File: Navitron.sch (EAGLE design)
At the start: 78 parts, among them J2 DX07S016JA1R1500, Q1 ROHM_RUM002N02T2LROHM_RUM002N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, Q2 2.5A/30V, Q3 ROHM_RUM002N02T2LROHM_RUM002N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, Q4 ROHM_RUM002N02T2LROHM_RUM002N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, Q5 ROHM_RUM002N02T2LROHM_RUM002N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, T1 BC847, T2 BC847, U1 ESP32-WROOM-32, U2 9DoF IMU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

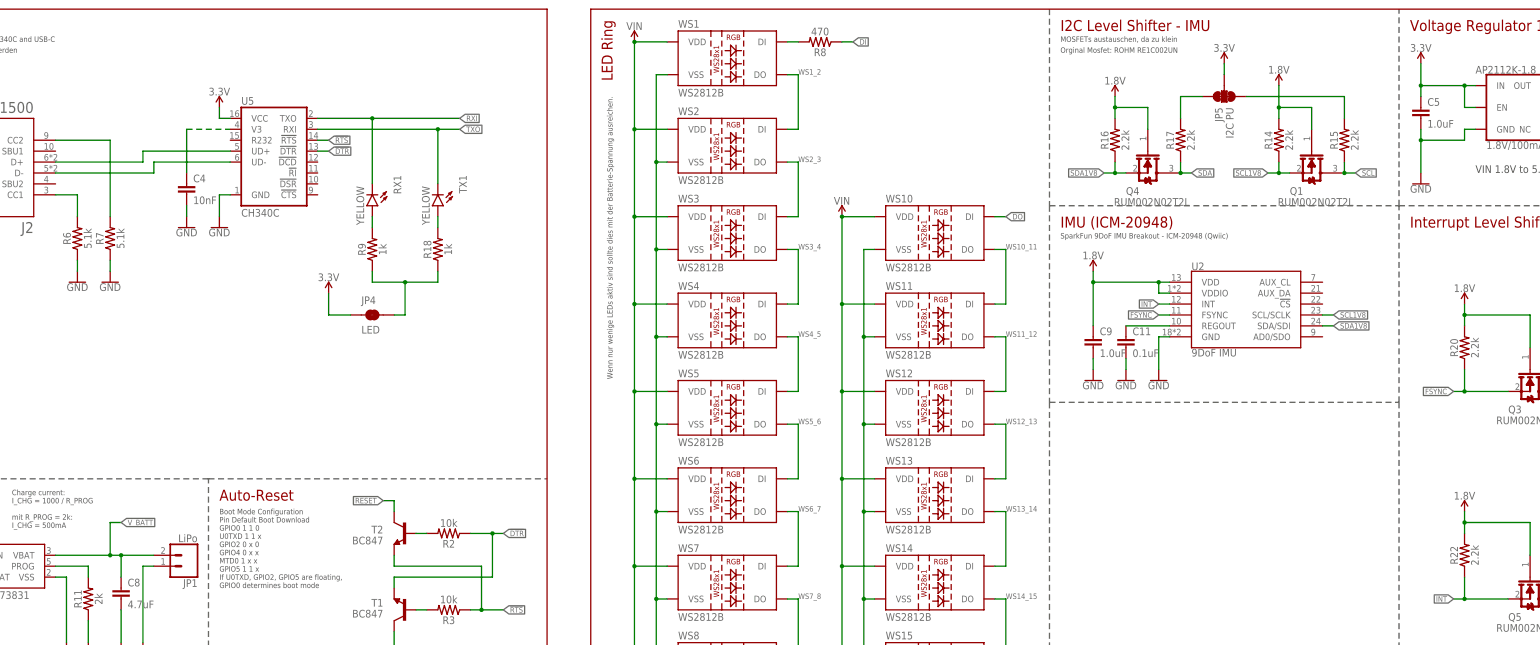
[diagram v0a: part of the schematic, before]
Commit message: Replace 403 Resistors with 603 Resistors
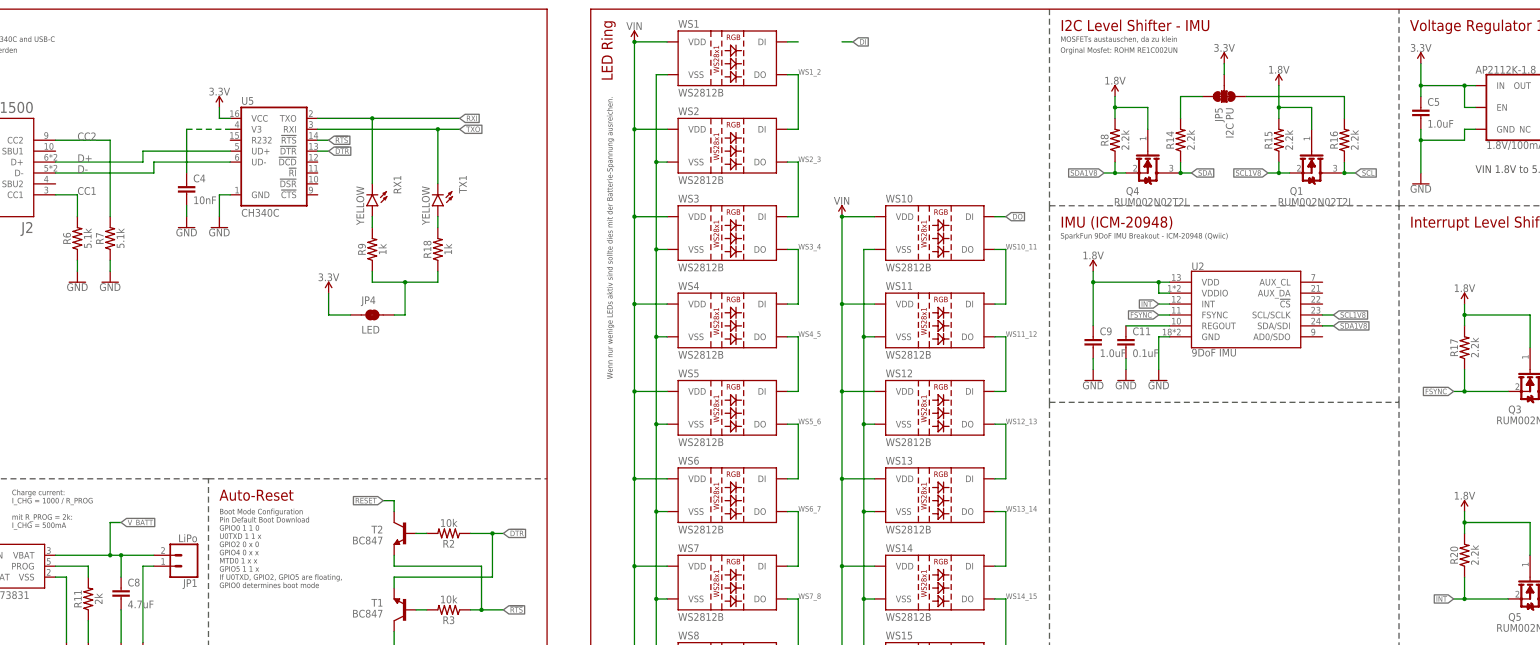
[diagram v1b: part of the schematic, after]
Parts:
- removed R22: 2.2k, SparkFun-Resistors:2.2KOHM-0402T-1/16W-1%
- R14, R15, R16, R17, R19, R20, R21: device SparkFun-Resistors:2.2KOHM-0402T-1/16W-1% -> SparkFun-Resistors:5.1KOHM5.1KOHM-0603-1/10W-1%
- R8: value 470 -> 2.2k; device SparkFun-Resistors:2.2KOHM-0402T-1/16W-1% -> SparkFun-Resistors:5.1KOHM5.1KOHM-0603-1/10W-1%
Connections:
- net N$31 renamed TO_RX_LED
- net N$32 renamed TO_TX_LED
- net N$33 renamed TX_RX_LED_SUPPLY
- net N$6 renamed V3_CH340
- net 1.8V: now also R15.2, R17.2, R8.2; no longer R14.2, R16.2, R22.2
- net DI: no longer R8.1
- net FSYNC: now also R17.1; no longer R20.1
- net INT: now also R20.1; no longer R22.1
- net N$10: no longer R8.2
- net N$14: now also R16.2; no longer R15.2
- net N$15: now also R14.2; no longer R17.2
- net SCL: now also R16.1; no longer R15.1
- net SCL1V8: now also R15.1; no longer R14.1
- net SDA: now also R14.1; no longer R17.1
- net SDA1V8: now also R8.1; no longer R16.1

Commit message: Update
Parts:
- removed S1: RESET, SparkFun-Switches:MOMENTARY-SWITCH-SPST-SMD-4.6X2.8MM
- removed S2: 0, SparkFun-Switches:MOMENTARY-SWITCH-SPST-SMD-4.6X2.8MM
- added U$1, U$2: MYSWITCH, MyLib:MYSWITCH
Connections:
- net 0: now also U$2.2; no longer S2.2
- net GND: now also U$1.1, U$2.1; no longer S1.1, S2.1
- net RESET: now also U$1.2; no longer S1.2
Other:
- moved on the sheet: AP2112K-1.8, C11, C12, C5, C9, JP3, JP5, POWER2, Q1, Q3, Q4, Q5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

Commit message: Inspected
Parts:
- added R22: 470, SparkFun-Resistors:5.1KOHM5.1KOHM-0603-1/10W-1%
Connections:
- net DO renamed WS9_10
- net N$16 renamed REGOUT
- net N$2 renamed CHAR_LED_VIN
- net N$3 renamed STAT
- net N$4 renamed TO_T2
- net N$5 renamed TO_T1
- net N$7 renamed PROG
- removed net N$10: WS1.DI
- new net DI_TO_WS: R22.1, WS1.DI
- net DI: now also R22.2
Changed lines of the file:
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@@
 <part name="U$1" library="MyLib" deviceset="MYSWITCH" device=""/>
 <part name="U$2" library="MyLib" deviceset="MYSWITCH" device=""/>
+<part name="R22" library="SparkFun-Resistors" deviceset="5.1KOHM" device="5.1KOHM-0603-1/10W-1%" value="470"/>
 </parts>
 <sheets>
@@
 <attribute name="VALUE" x="139.7" y="12.192" size="1.778" layer="96" font="vector" align="top-center"/>
 </instance>
+<instance part="R22" gate="R1" x="53.34" y="-53.34" smashed="yes">
+<attribute name="NAME" x="53.34" y="-51.816" size="1.778" layer="95" font="vector" align="bottom-center"/>
+<attribute name="VALUE" x="53.34" y="-54.864" size="1.778" layer="96" font="vector" align="top-center"/>
+</instance>
 </instances>
 <busses>
@@
 </segment>
 </net>
-<net name="N$4" class="0">
+<net name="TO_T2" class="0">
 <segment>
 <pinref part="R2" gate="G$1" pin="2"/>
@@
 </segment>
 </net>
-<net name="N$5" class="0">
+<net name="TO_T1" class="0">
 <segment>
 <pinref part="R3" gate="G$1" pin="2"/>
@@
 </segment>
 </net>
-<net name="N$2" class="0">
+<net name="CHAR_LED_VIN" class="0">
 <segment>
 <pinref part="CHARGING" gate="G$1" pin="A"/>
@@
 </segment>
 </net>
-<net name="N$3" class="0">
+<net name="STAT" class="0">
 <segment>
 <pinref part="CHARGING" gate="G$1" pin="C"/>
@@
 </segment>
 </net>
-<net name="N$7" class="0">
+<net name="PROG" class="0">
 <segment>
 <pinref part="R11" gate="R1" pin="2"/>
@@
 </segment>
 </net>
-<net name="N$16" class="0">
+<net name="REGOUT" class="0">
 <segment>
 <pinref part="C11" gate="G$1" pin="1"/>
@@
 <wire x1="58.42" y1="-53.34" x2="60.96" y2="-53.34" width="0.1524" layer="91"/>
 <label x="60.96" y="-53.34" size="1.27" layer="95" xref="yes"/>
+<pinref part="R22" gate="R1" pin="2"/>
 </segment>
 </net>
@@
 </segment>
 </net>
-<net name="DO" class="0">
+<net name="WS9_10" class="0">
 <segment>
 <pinref part="WS9" gate="G$1" pin="DO"/>
@@
 </segment>
 </net>
-<net name="N$10" class="0">
+<net name="DI_TO_WS" class="0">
 <segment>
 <pinref part="WS1" gate="G$1" pin="DI"/>
 <wire x1="48.26" y1="-53.34" x2="45.72" y2="-53.34" width="0.1524" layer="91"/>
+<pinref part="R22" gate="R1" pin="1"/>
 </segment>
 </net>
@@
 </sheet>
 </sheets>
-<errors>
-</errors>
 </schematic>
 </drawing>

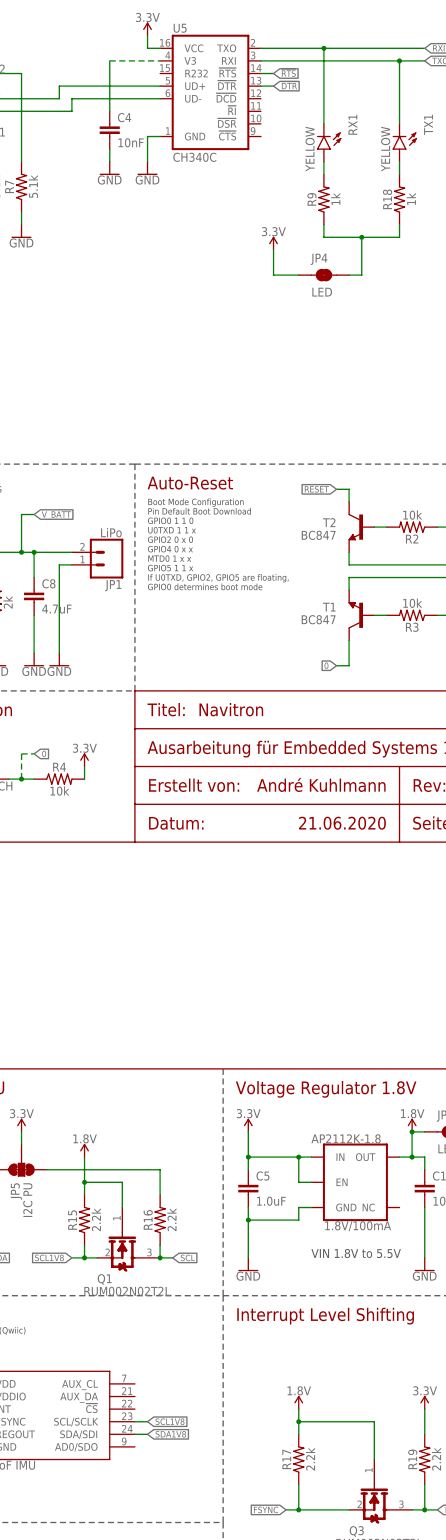
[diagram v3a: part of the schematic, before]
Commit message: Pad Renaming
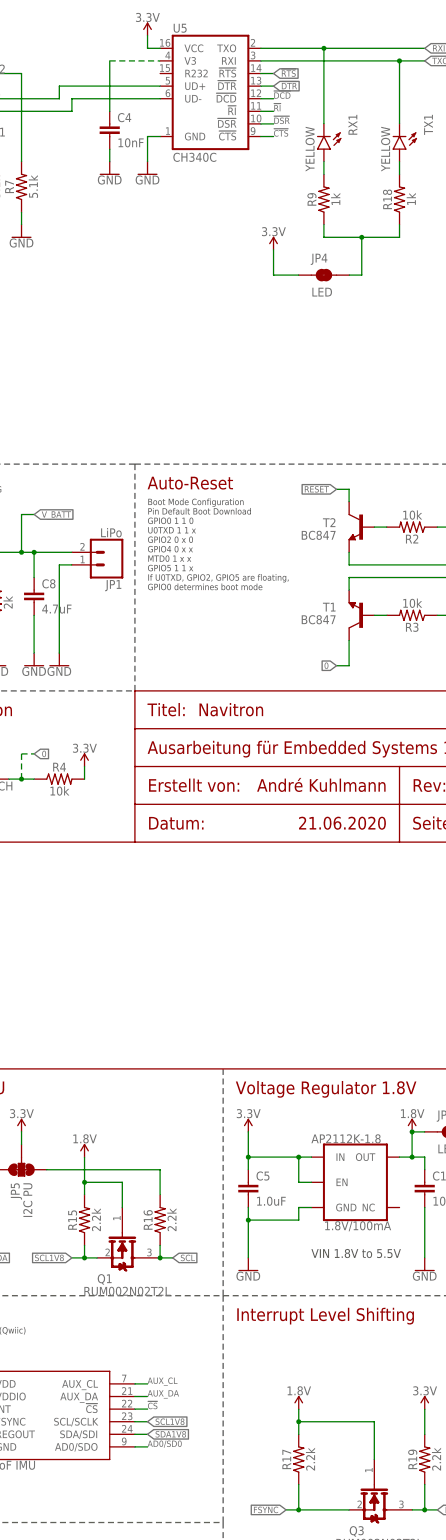
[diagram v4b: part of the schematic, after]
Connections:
- net N$12 renamed LED1.8_2
- net N$13 renamed LED1.8
- net N$14 renamed SDA_W_2
- net N$15 renamed SDA_W_1
- new net !CS: U2.!CS
- new net !CTS: U5.!CTS
- new net !DCD: U5.!DCD
- new net !DSR: U5.!DSR
- new net !RI: U5.!RI
- new net AD0/SD0: U2.AD0/SDO
- new net AUX_CL: U2.AUX_CL
- new net AUX_DA: U2.AUX_DA
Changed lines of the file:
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@@
 </segment>
 </net>
-<net name="N$12" class="0">
+<net name="LED1.8_2" class="0">
 <segment>
 <pinref part="R12" gate="G$1" pin="2"/>
@@
 </segment>
 </net>
-<net name="N$13" class="0">
+<net name="LED1.8" class="0">
 <segment>
 <pinref part="POWER2" gate="G$1" pin="A"/>
@@
 </segment>
 </net>
-<net name="N$14" class="0">
+<net name="SDA_W_2" class="0">
 <segment>
 <wire x1="175.26" y1="-66.04" x2="175.26" y2="-71.12" width="0.1524" layer="91"/>
@@
 </segment>
 </net>
-<net name="N$15" class="0">
+<net name="SDA_W_1" class="0">
 <segment>
 <wire x1="137.16" y1="-71.12" x2="137.16" y2="-66.04" width="0.1524" layer="91"/>
@@
 </segment>
 </net>
+<net name="AUX_CL" class="0">
+<segment>
+<pinref part="U2" gate="G$1" pin="AUX_CL"/>
+<wire x1="170.18" y1="-109.22" x2="172.72" y2="-109.22" width="0.1524" layer="91"/>
+<label x="172.72" y="-109.22" size="1.27" layer="95"/>
+</segment>
+</net>
+<net name="AUX_DA" class="0">
+<segment>
+<pinref part="U2" gate="G$1" pin="AUX_DA"/>
+<wire x1="170.18" y1="-111.76" x2="172.72" y2="-111.76" width="0.1524" layer="91"/>
+<label x="172.72" y="-111.76" size="1.27" layer="95"/>
+</segment>
+</net>
+<net name="!CS" class="0">
+<segment>
+<pinref part="U2" gate="G$1" pin="!CS"/>
+<wire x1="170.18" y1="-114.3" x2="172.72" y2="-114.3" width="0.1524" layer="91"/>
+<label x="172.72" y="-114.3" size="1.27" layer="95"/>
+</segment>
+</net>
+<net name="AD0/SD0" class="0">
+<segment>
+<pinref part="U2" gate="G$1" pin="AD0/SDO"/>
+<wire x1="170.18" y1="-121.92" x2="172.72" y2="-121.92" width="0.1524" layer="91"/>
+<label x="172.72" y="-121.92" size="1.27" layer="95"/>
+</segment>
+</net>
+<net name="!DCD" class="0">
+<segment>
+<pinref part="U5" gate="U1" pin="!DCD"/>
+<wire x1="195.58" y1="149.86" x2="198.12" y2="149.86" width="0.1524" layer="91"/>
+<label x="198.12" y="149.86" size="1.27" layer="95"/>
+</segment>
+</net>
+<net name="!RI" class="0">
+<segment>
+<pinref part="U5" gate="U1" pin="!RI"/>
+<wire x1="195.58" y1="147.32" x2="198.12" y2="147.32" width="0.1524" layer="91"/>
+<label x="198.12" y="147.32" size="1.27" layer="95"/>
+</segment>
+</net>
+<net name="!DSR" class="0">
+<segment>
+<pinref part="U5" gate="U1" pin="!DSR"/>
+<wire x1="195.58" y1="144.78" x2="198.12" y2="144.78" width="0.1524" layer="91"/>
+<label x="198.12" y="144.78" size="1.27" layer="95"/>
+</segment>
+</net>
+<net name="!CTS" class="0">
+<segment>
+<pinref part="U5" gate="U1" pin="!CTS"/>
+<wire x1="195.58" y1="142.24" x2="198.12" y2="142.24" width="0.1524" layer="91"/>
+<label x="198.12" y="142.24" size="1.27" layer="95"/>
+</segment>
+</net>

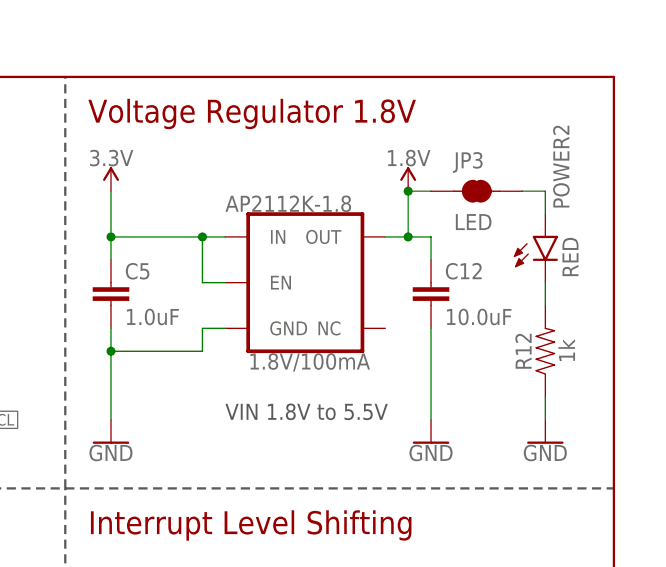
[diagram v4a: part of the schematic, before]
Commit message: Change Voltage Regulator and Resistor Value
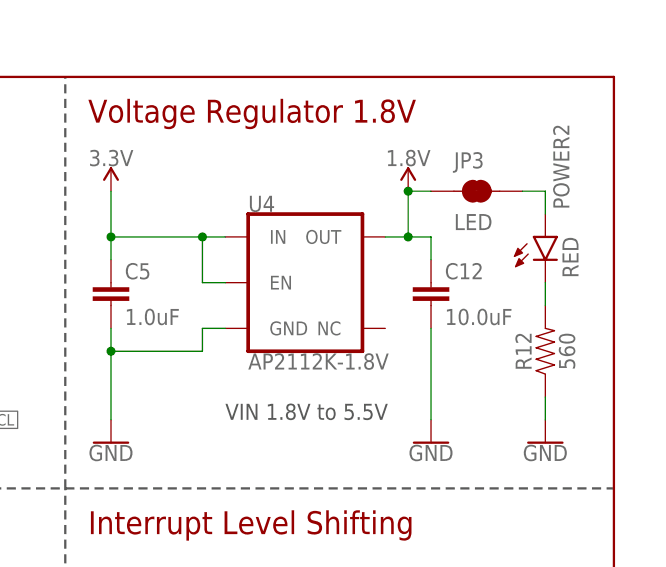
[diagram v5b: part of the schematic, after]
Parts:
- removed AP2112K-1.8: 1.8V/100mA, SparkFun-IC-Power:V_REG_SP6214-1.8V
- added U4: AP2112K-1.8V, SparkFun-IC-Power-Customized:V_REG_AP2112K-1.8V
- R12: value 1k -> 560
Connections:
- net 1.8V: now also U4.OUT; no longer AP2112K-1.8.OUT
- net 3.3V: now also U4.EN, U4.IN; no longer AP2112K-1.8.EN, AP2112K-1.8.IN
- net GND: now also U4.GND; no longer AP2112K-1.8.GND
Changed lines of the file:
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@@
 <part name="GND25" library="SparkFun-PowerSymbols" deviceset="GND" device=""/>
 <part name="U2" library="SparkFun-Sensors" deviceset="MPU-9250" device="" value="9DoF IMU"/>
-<part name="AP2112K-1.8" library="SparkFun-IC-Power" deviceset="V_REG_SP6214" device="-1.8V" value="1.8V/100mA"/>
 <part name="GND14" library="SparkFun-PowerSymbols" deviceset="GND" device=""/>
 <part name="SUPPLY11" library="SparkFun-PowerSymbols" deviceset="1.8V" device=""/>
@@
 <part name="GND18" library="SparkFun-PowerSymbols" deviceset="GND" device=""/>
 <part name="POWER2" library="SparkFun-LED" deviceset="LED-RED" device="0603" value="RED"/>
-<part name="R12" library="SparkFun-Resistors" deviceset="10MOHM" device="-0603-1/10W-5%" value="1k"/>
+<part name="R12" library="SparkFun-Resistors" deviceset="10MOHM" device="-0603-1/10W-5%" value="560"/>
 <part name="GND26" library="SparkFun-PowerSymbols" deviceset="GND" device=""/>
 <part name="JP3" library="SparkFun-Jumpers" deviceset="JUMPER-SMT_2_NC_TRACE" device="_SILK" value="LED"/>
@@
 <part name="U$2" library="MyLib" deviceset="MYSWITCH" device=""/>
 <part name="R22" library="SparkFun-Resistors" deviceset="5.1KOHM" device="5.1KOHM-0603-1/10W-1%" value="470"/>
+<part name="U4" library="SparkFun-IC-Power-Customized" deviceset="V_REG_AP2112" device="K-1.8V" package3d_urn="urn:adsk.eagle:package:39060/1" value="AP2112K-1.8V"/>
 </parts>
 <sheets>
@@
 <attribute name="VALUE" x="139.7" y="-124.714" size="1.778" layer="96" font="vector" align="top-left"/>
 </instance>
-<instance part="AP2112K-1.8" gate="G$1" x="215.9" y="-68.58" smashed="yes">
-<attribute name="NAME" x="205.74" y="-60.706" size="1.778" layer="95" font="vector"/>
-<attribute name="VALUE" x="208.28" y="-76.454" size="1.778" layer="96" font="vector" align="top-left"/>
-</instance>
 <instance part="GND14" gate="1" x="193.04" y="-86.36" smashed="yes">
 <attribute name="VALUE" x="193.04" y="-86.614" size="1.778" layer="96" align="top-center"/>
@@
 <attribute name="NAME" x="53.34" y="-51.816" size="1.778" layer="95" font="vector" align="bottom-center"/>
 <attribute name="VALUE" x="53.34" y="-54.864" size="1.778" layer="96" font="vector" align="top-center"/>
+</instance>
+<instance part="U4" gate="G$1" x="215.9" y="-68.58" smashed="yes">
+<attribute name="NAME" x="208.28" y="-60.706" size="1.778" layer="95" font="vector"/>
+<attribute name="VALUE" x="208.28" y="-76.454" size="1.778" layer="96" font="vector" align="top-left"/>
 </instance>
 </instances>
@@
 </segment>
 <segment>
-<pinref part="AP2112K-1.8" gate="G$1" pin="GND"/>
 <wire x1="205.74" y1="-73.66" x2="203.2" y2="-73.66" width="0.1524" layer="91"/>
 <wire x1="203.2" y1="-73.66" x2="203.2" y2="-76.2" width="0.1524" layer="91"/>
@@
 <junction x="193.04" y="-76.2"/>
 <pinref part="C5" gate="G$1" pin="2"/>
+<pinref part="U4" gate="G$1" pin="GND"/>
 </segment>
 <segment>
@@
 <segment>
 <wire x1="193.04" y1="-58.42" x2="193.04" y2="-63.5" width="0.1524" layer="91"/>
-<pinref part="AP2112K-1.8" gate="G$1" pin="IN"/>
 <wire x1="193.04" y1="-63.5" x2="193.04" y2="-66.04" width="0.1524" layer="91"/>
 <wire x1="205.74" y1="-63.5" x2="203.2" y2="-63.5" width="0.1524" layer="91"/>
 <junction x="193.04" y="-63.5"/>
-<pinref part="AP2112K-1.8" gate="G$1" pin="EN"/>
 <wire x1="203.2" y1="-63.5" x2="193.04" y2="-63.5" width="0.1524" layer="91"/>
 <wire x1="205.74" y1="-68.58" x2="203.2" y2="-68.58" width="0.1524" layer="91"/>
@@
 <pinref part="SUPPLY10" gate="G$1" pin="3.3V"/>
 <pinref part="C5" gate="G$1" pin="1"/>
+<pinref part="U4" gate="G$1" pin="IN"/>
+<pinref part="U4" gate="G$1" pin="EN"/>
 </segment>
 <segment>
@@
 <pinref part="JP3" gate="G$1" pin="1"/>
 <wire x1="228.6" y1="-58.42" x2="226.06" y2="-58.42" width="0.1524" layer="91"/>
-<pinref part="AP2112K-1.8" gate="G$1" pin="OUT"/>
 <wire x1="223.52" y1="-63.5" x2="226.06" y2="-63.5" width="0.1524" layer="91"/>
 <wire x1="226.06" y1="-63.5" x2="226.06" y2="-58.42" width="0.1524" layer="91"/>
@@
 <pinref part="C12" gate="G$1" pin="1"/>
 <wire x1="228.6" y1="-63.5" x2="228.6" y2="-66.04" width="0.1524" layer="91"/>
-</segment>
-<segment>
+<pinref part="U4" gate="G$1" pin="OUT"/>
+</segment>
+<segment>
